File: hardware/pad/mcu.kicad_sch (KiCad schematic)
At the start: 2 parts, among them J4 SWD

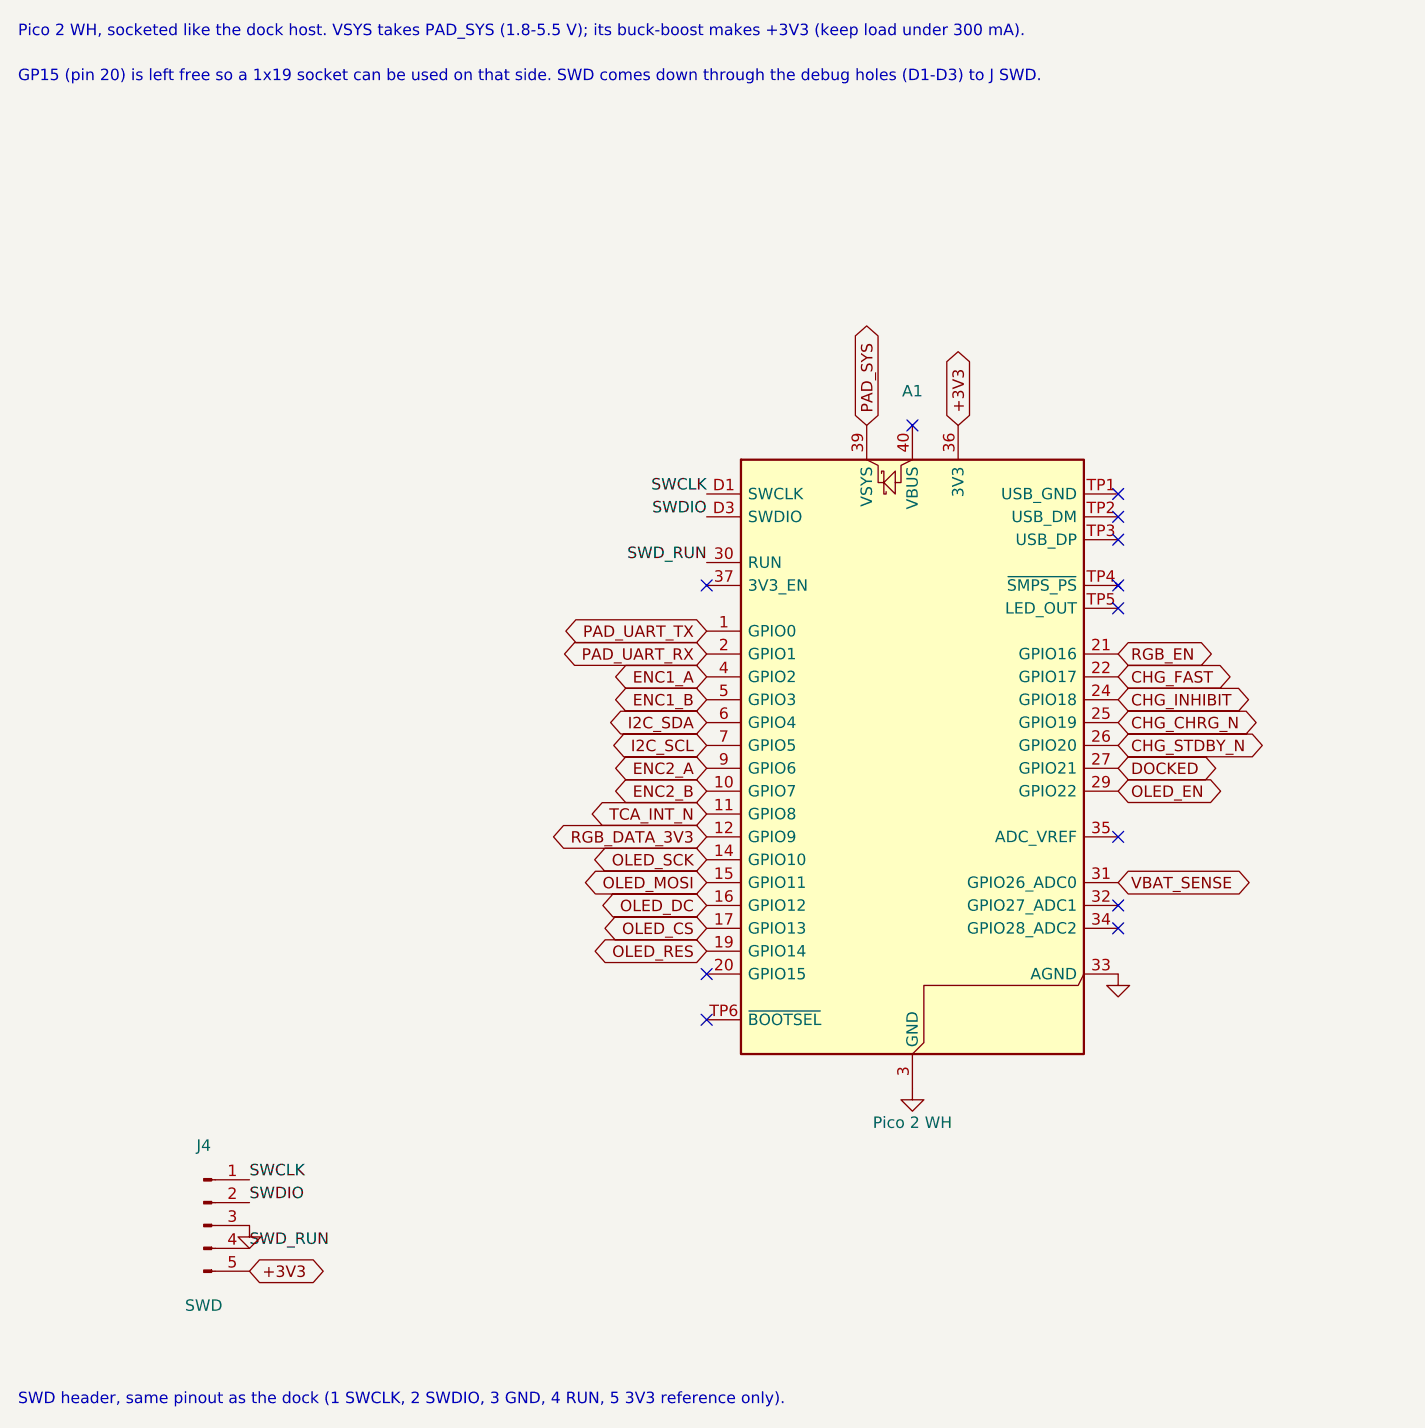
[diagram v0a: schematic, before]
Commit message: Pad schematic: hand-redrawn from the connection guide; netlist verified against the reference
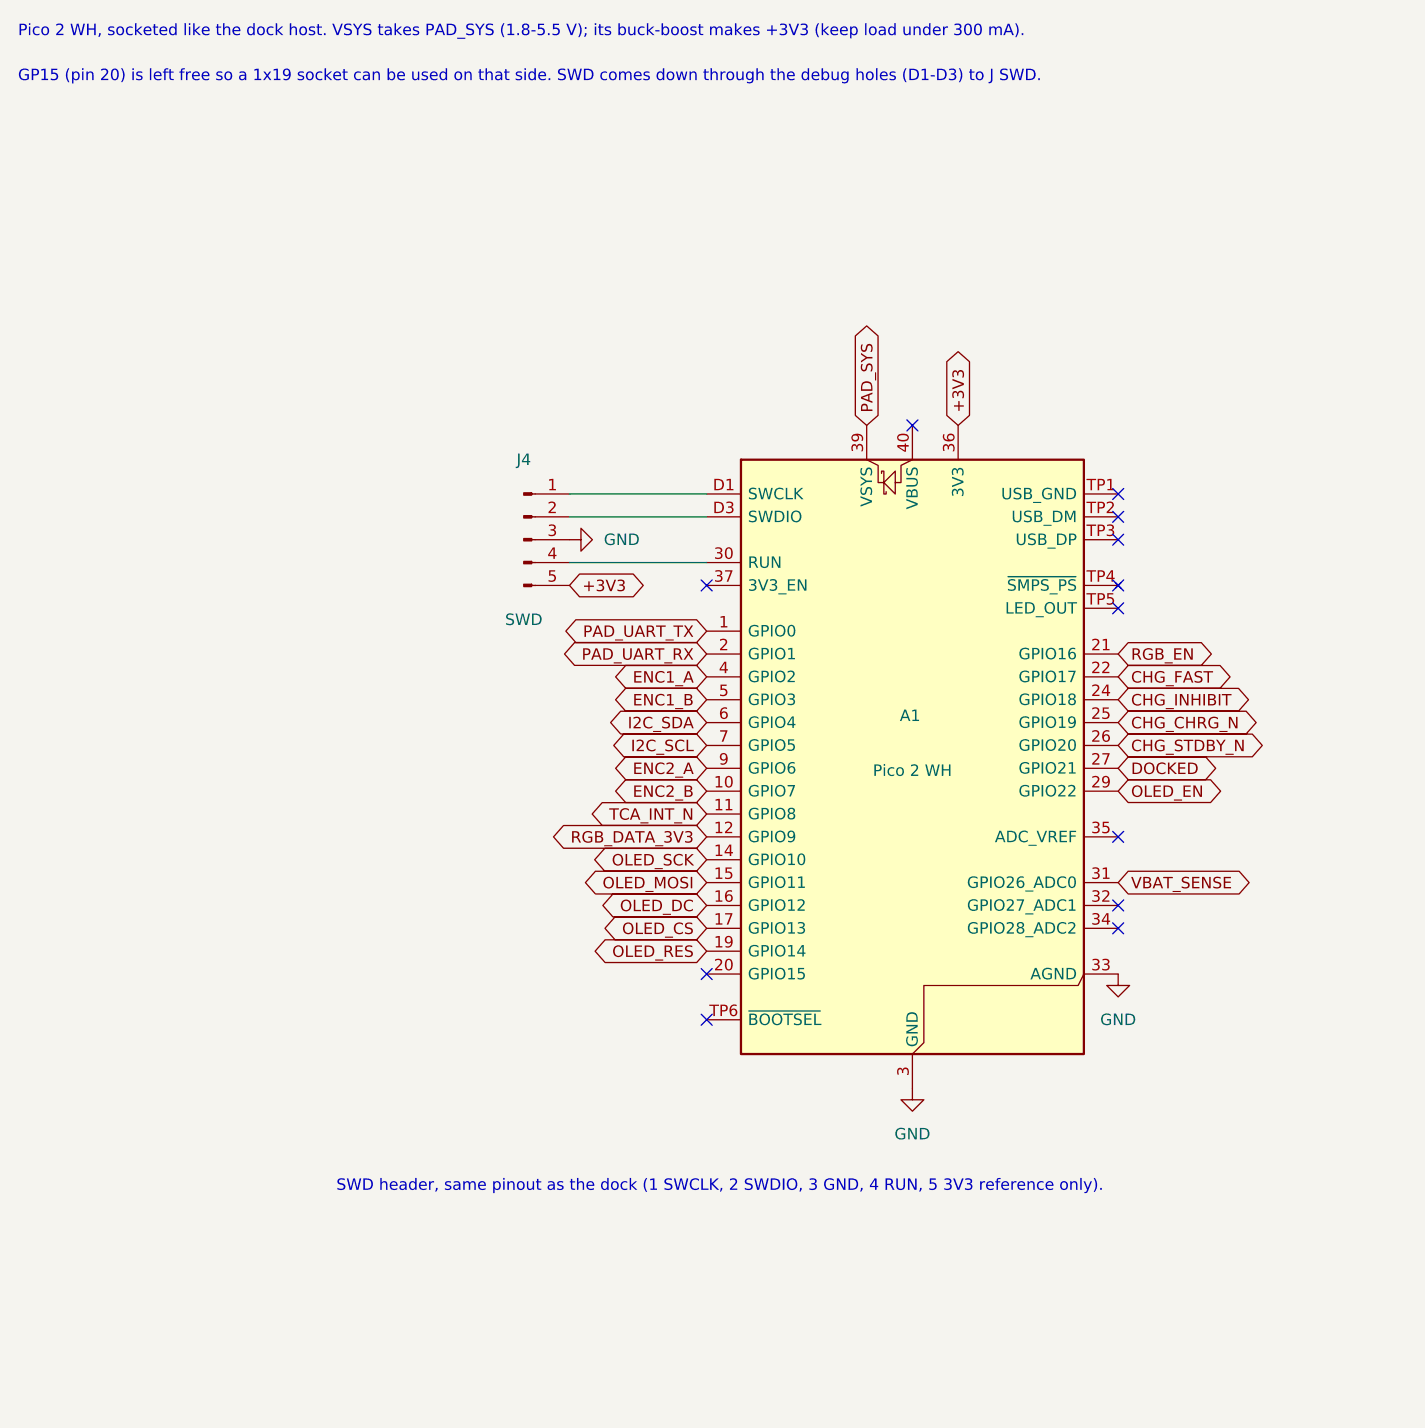
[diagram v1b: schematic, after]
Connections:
- net SWCLK: no longer names the net of A1.D1 (SWCLK), J4.1 (Pin_1)
- net SWDIO: no longer names the net of A1.D3 (SWDIO), J4.2 (Pin_2)
- net SWD_RUN: no longer names the net of A1.30 (RUN), J4.4 (Pin_4)
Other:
- moved on the sheet: J4
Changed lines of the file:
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@@
 	(text "SWD header, same pinout as the dock (1 SWCLK, 2 SWDIO, 3 GND, 4 RUN, 5 3V3 reference only)."
 		(exclude_from_sim no)
-		(at 20 170 0)
+		(at 55.372 146.304 0)
 		(effects
 			(font
@@
 		(at 96.52 127)
 	)
-	(label "SWD_RUN"
-		(at 96.52 76.2 180)
-		(effects
-			(font
-				(size 1.27 1.27)
-			)
-			(justify right bottom)
-		)
-	)
-	(label "SWCLK"
-		(at 45.72 144.78 0)
-		(effects
-			(font
-				(size 1.27 1.27)
-			)
-			(justify left bottom)
-		)
-	)
-	(label "SWDIO"
-		(at 96.52 71.12 180)
-		(effects
-			(font
-				(size 1.27 1.27)
-			)
-			(justify right bottom)
-		)
-	)
-	(label "SWDIO"
-		(at 45.72 147.32 0)
-		(effects
-			(font
-				(size 1.27 1.27)
-			)
-			(justify left bottom)
-		)
-	)
-	(label "SWCLK"
-		(at 96.52 68.58 180)
-		(effects
-			(font
-				(size 1.27 1.27)
-			)
-			(justify right bottom)
-		)
-	)
-	(label "SWD_RUN"
-		(at 45.72 152.4 0)
-		(effects
-			(font
-				(size 1.27 1.27)
-			)
-			(justify left bottom)
+	(wire
+		(pts
+			(xy 81.28 76.2) (xy 96.52 76.2)
+		)
+		(stroke
+			(width 0)
+			(type default)
+		)
+	)
+	(wire
+		(pts
+			(xy 81.28 68.58) (xy 96.52 68.58)
+		)
+		(stroke
+			(width 0)
+			(type default)
+		)
+	)
+	(wire
+		(pts
+			(xy 81.28 71.12) (xy 96.52 71.12)
+		)
+		(stroke
+			(width 0)
+			(type default)
 		)
 	)
@@
 	(global_label "+3V3"
 		(shape bidirectional)
-		(at 45.72 154.94 0)
+		(at 81.28 78.74 0)
 		(fields_autoplaced yes)
 		(effects
@@
 		)
 		(property "Intersheetrefs" "${INTERSHEET_REFS}"
-			(at 45.72 154.94 0)
+			(at 81.28 78.74 0)
 			(hide yes)
 			(show_name no)
@@
 		(dnp no)
 		(property "Reference" "A1"
-			(at 119.38 57.15 0)
+			(at 119.126 93.218 0)
 			(show_name no)
 			(do_not_autoplace no)
@@
 		)
 		(property "Value" "Pico 2 WH"
-			(at 119.38 138.43 0)
+			(at 119.38 99.314 0)
 			(show_name no)
 			(do_not_autoplace no)
@@
 		(in_pos_files yes)
 		(dnp no)
-		(property "Reference" "#PWR034"
+		(fields_autoplaced yes)
+		(property "Reference" "#PWR020"
 			(at 142.24 128.27 0)
 			(hide yes)
@@
 		)
 		(property "Value" "GND"
-			(at 142.24 125.73 0)
-			(hide yes)
+			(at 142.24 127 0)
 			(show_name no)
 			(do_not_autoplace no)
@@
 		(property "Footprint" ""
 			(at 142.24 121.92 0)
+			(hide yes)
 			(show_name no)
 			(do_not_autoplace no)
@@
 		(property "Datasheet" ""
 			(at 142.24 121.92 0)
-			(show_name no)
-			(do_not_autoplace no)
-			(effects
-				(font
-					(size 1.27 1.27)
-				)
-			)
-		)
-		(property "Description" ""
+			(hide yes)
+			(show_name no)
+			(do_not_autoplace no)
+			(effects
+				(font
+					(size 1.27 1.27)
+				)
+			)
+		)
+		(property "Description" "Power symbol creates a global label with name \"GND\" , ground"
 			(at 142.24 121.92 0)
+			(hide yes)
 			(show_name no)
 			(do_not_autoplace no)
@@
 			(project "pad"
 				(path "/e7f715eb-7c18-4c70-befb-dbed60a95ef2/f913b2b7-06cc-4745-bf8c-45e5b76c74d5"
-					(reference "#PWR034")
+					(reference "#PWR020")
 					(unit 1)
 				)
@@
 	(symbol
 		(lib_id "power:GND")
-		(at 45.72 149.86 0)
+		(at 81.28 73.66 90)
 		(unit 1)
 		(body_style 1)
@@
 		(in_pos_files yes)
 		(dnp no)
-		(property "Reference" "#PWR035"
-			(at 45.72 156.21 0)
+		(fields_autoplaced yes)
+		(property "Reference" "#PWR019"
+			(at 87.63 73.66 0)
 			(hide yes)
 			(show_name no)
@@
 		)
 		(property "Value" "GND"
-			(at 45.72 153.67 0)
-			(hide yes)
-			(show_name no)
-			(do_not_autoplace no)
-			(effects
-				(font
-					(size 1.27 1.27)
-				)
+			(at 85.09 73.6599 90)
+			(show_name no)
+			(do_not_autoplace no)
+			(effects
+				(font
+					(size 1.27 1.27)
+				)
+				(justify right)
 			)
 		)
 		(property "Footprint" ""
-			(at 45.72 149.86 0)
+			(at 81.28 73.66 0)
+			(hide yes)
 			(show_name no)
 			(do_not_autoplace no)
@@
 		)
 		(property "Datasheet" ""
-			(at 45.72 149.86 0)
-			(show_name no)
-			(do_not_autoplace no)
-			(effects
-				(font
-					(size 1.27 1.27)
-				)
-			)
-		)
-		(property "Description" ""
-			(at 45.72 149.86 0)
+			(at 81.28 73.66 0)
+			(hide yes)
+			(show_name no)
+			(do_not_autoplace no)
+			(effects
+				(font
+					(size 1.27 1.27)
+				)
+			)
+		)
+		(property "Description" "Power symbol creates a global label with name \"GND\" , ground"
+			(at 81.28 73.66 0)
+			(hide yes)
 			(show_name no)
 			(do_not_autoplace no)
@@
 			(project "pad"
 				(path "/e7f715eb-7c18-4c70-befb-dbed60a95ef2/f913b2b7-06cc-4745-bf8c-45e5b76c74d5"
-					(reference "#PWR035")
+					(reference "#PWR019")
 					(unit 1)
 				)
@@
 	(symbol
 		(lib_id "Connector:Conn_01x05_Pin")
-		(at 40.64 149.86 0)
+		(at 76.2 73.66 0)
 		(unit 1)
 		(body_style 1)
@@
 		(dnp no)
 		(property "Reference" "J4"
-			(at 40.64 140.97 0)
+			(at 76.2 64.77 0)
 			(show_name no)
 			(do_not_autoplace no)
@@
 		)
 		(property "Value" "SWD"
-			(at 40.64 158.75 0)
+			(at 76.2 82.55 0)
 			(show_name no)
 			(do_not_autoplace no)
@@
 		)
 		(property "Footprint" "Connector_PinHeader_2.54mm:PinHeader_1x05_P2.54mm_Vertical"
-			(at 40.64 149.86 0)
+			(at 76.2 73.66 0)
 			(hide yes)
 			(show_name no)
@@
 		)
 		(property "Datasheet" ""
-			(at 40.64 149.86 0)
+			(at 76.2 73.66 0)
 			(hide yes)
 			(show_name no)
@@
 		)
 		(property "Description" "Generic connector, single row, 01x05, script generated"
-			(at 40.64 149.86 0)
+			(at 76.2 73.66 0)
 			(hide yes)
 			(show_name no)
@@
 		(in_pos_files yes)
 		(dnp no)
-		(property "Reference" "#PWR033"
+		(fields_autoplaced yes)
+		(property "Reference" "#PWR021"
 			(at 119.38 140.97 0)
 			(hide yes)
@@
 		)
 		(property "Value" "GND"
-			(at 119.38 138.43 0)
-			(hide yes)
+			(at 119.38 139.7 0)
 			(show_name no)
 			(do_not_autoplace no)
@@
 		(property "Footprint" ""
 			(at 119.38 134.62 0)
+			(hide yes)
 			(show_name no)
 			(do_not_autoplace no)
@@
 		(property "Datasheet" ""
 			(at 119.38 134.62 0)
-			(show_name no)
-			(do_not_autoplace no)
-			(effects
-				(font
-					(size 1.27 1.27)
-				)
-			)
-		)
-		(property "Description" ""
+			(hide yes)
+			(show_name no)
+			(do_not_autoplace no)
+			(effects
+				(font
+					(size 1.27 1.27)
+				)
+			)
+		)
+		(property "Description" "Power symbol creates a global label with name \"GND\" , ground"
 			(at 119.38 134.62 0)
+			(hide yes)
 			(show_name no)
 			(do_not_autoplace no)
@@
 			(project "pad"
 				(path "/e7f715eb-7c18-4c70-befb-dbed60a95ef2/f913b2b7-06cc-4745-bf8c-45e5b76c74d5"
-					(reference "#PWR033")
+					(reference "#PWR021")
 					(unit 1)
 				)
